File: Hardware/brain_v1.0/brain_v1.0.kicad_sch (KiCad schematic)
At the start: 77 parts, among them J1 Conn_01x02, J10 RFID, J11 Conn_01x04, J12 Conn_01x04, J15 Conn_01x05, J2 Conn_01x02, J3 Conn_01x03, J4 JTAG, J5 Conn_01x02, J6 UART, J7 Conn_01x03, J8 UART Backup, J9 Conn_01x02, Q1 BSS138, Q2 BSS138, Q3 SMD-TRANSISTORS-NPN-25V-500MW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, Q4 SMD-TRANSISTORS-NPN-25V-500MW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, Q5 BSS138, Q6 BSS138, SW1 SW_Push, SW2 SW_Push, U1 ESP32-WROOM-32E 4MB, U2 NAU7802SGI

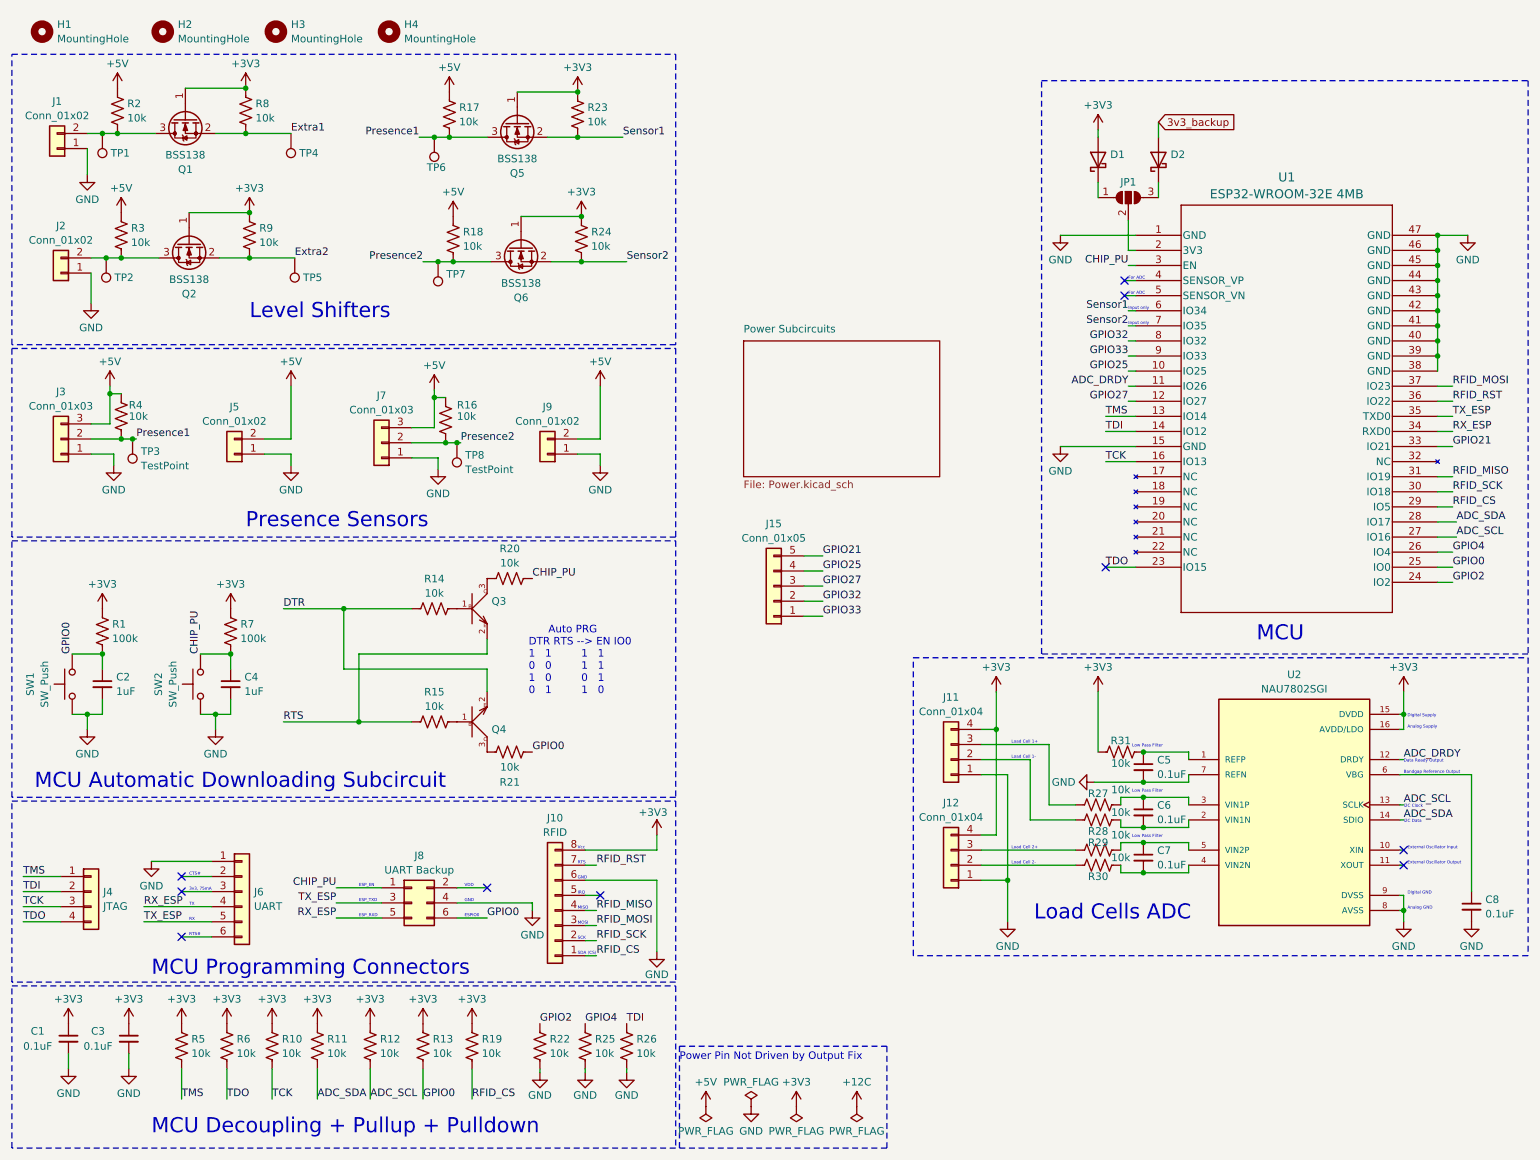
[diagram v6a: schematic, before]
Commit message: made motor driver layout base and moved brain power to a separate board
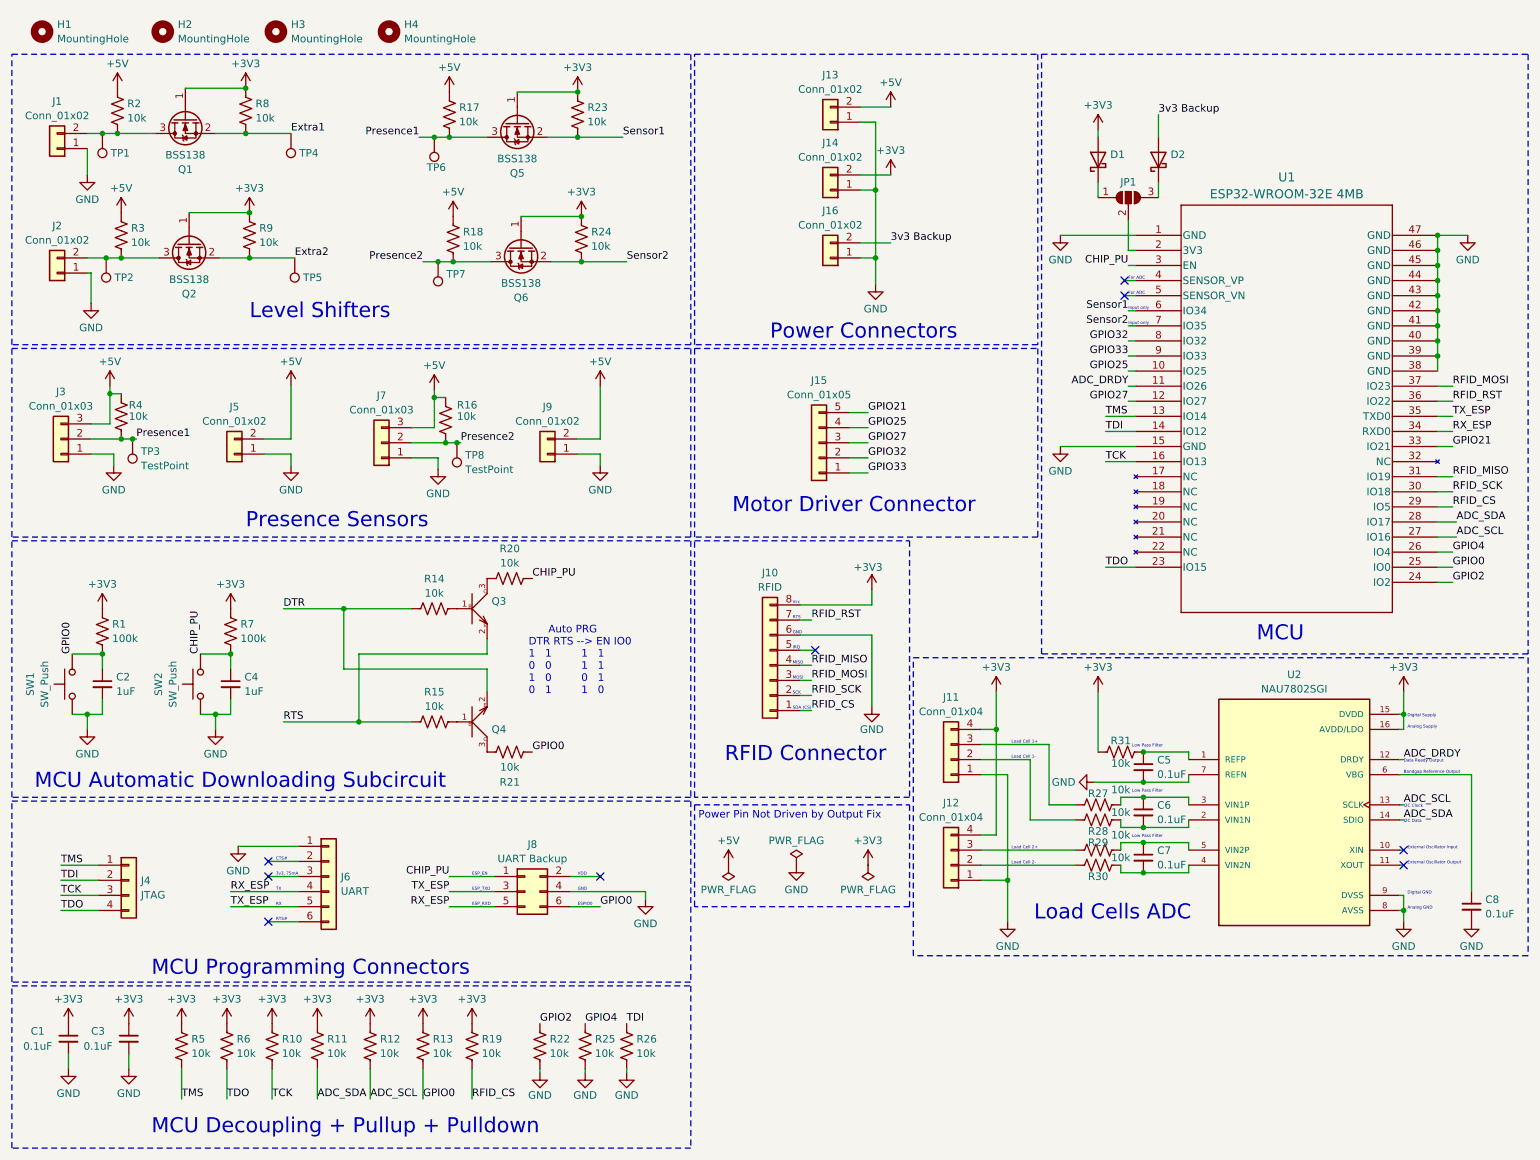
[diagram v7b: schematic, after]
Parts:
- added J13, J14, J16: Conn_01x02, Connector_Molex:Molex_KK-254_AE-6410-02A_1x02_P2.54mm_Vertical, symbol Connector_Generic:Conn_01x02
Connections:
- net +3V3: now also J14.2 (Pin_2)
- net +5V: now also J13.2 (Pin_2)
- net GND: now also J13.1 (Pin_1), J14.1 (Pin_1), J16.1 (Pin_1)
- net 3v3_backup renamed 3v3 Backup
- net 3v3 Backup: now also J16.2 (Pin_2)
- no-connect marks 10 -> 9
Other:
- removed sheet Power Subcircuits
- note added: "Motor Driver Connector"
- note added: "Power Connectors"
- note added: "RFID Connector"
- moved on the sheet: J10, J15, J2, J4, J6, J8

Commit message: started brain layout, can definitely be done in the 100x100 mm space
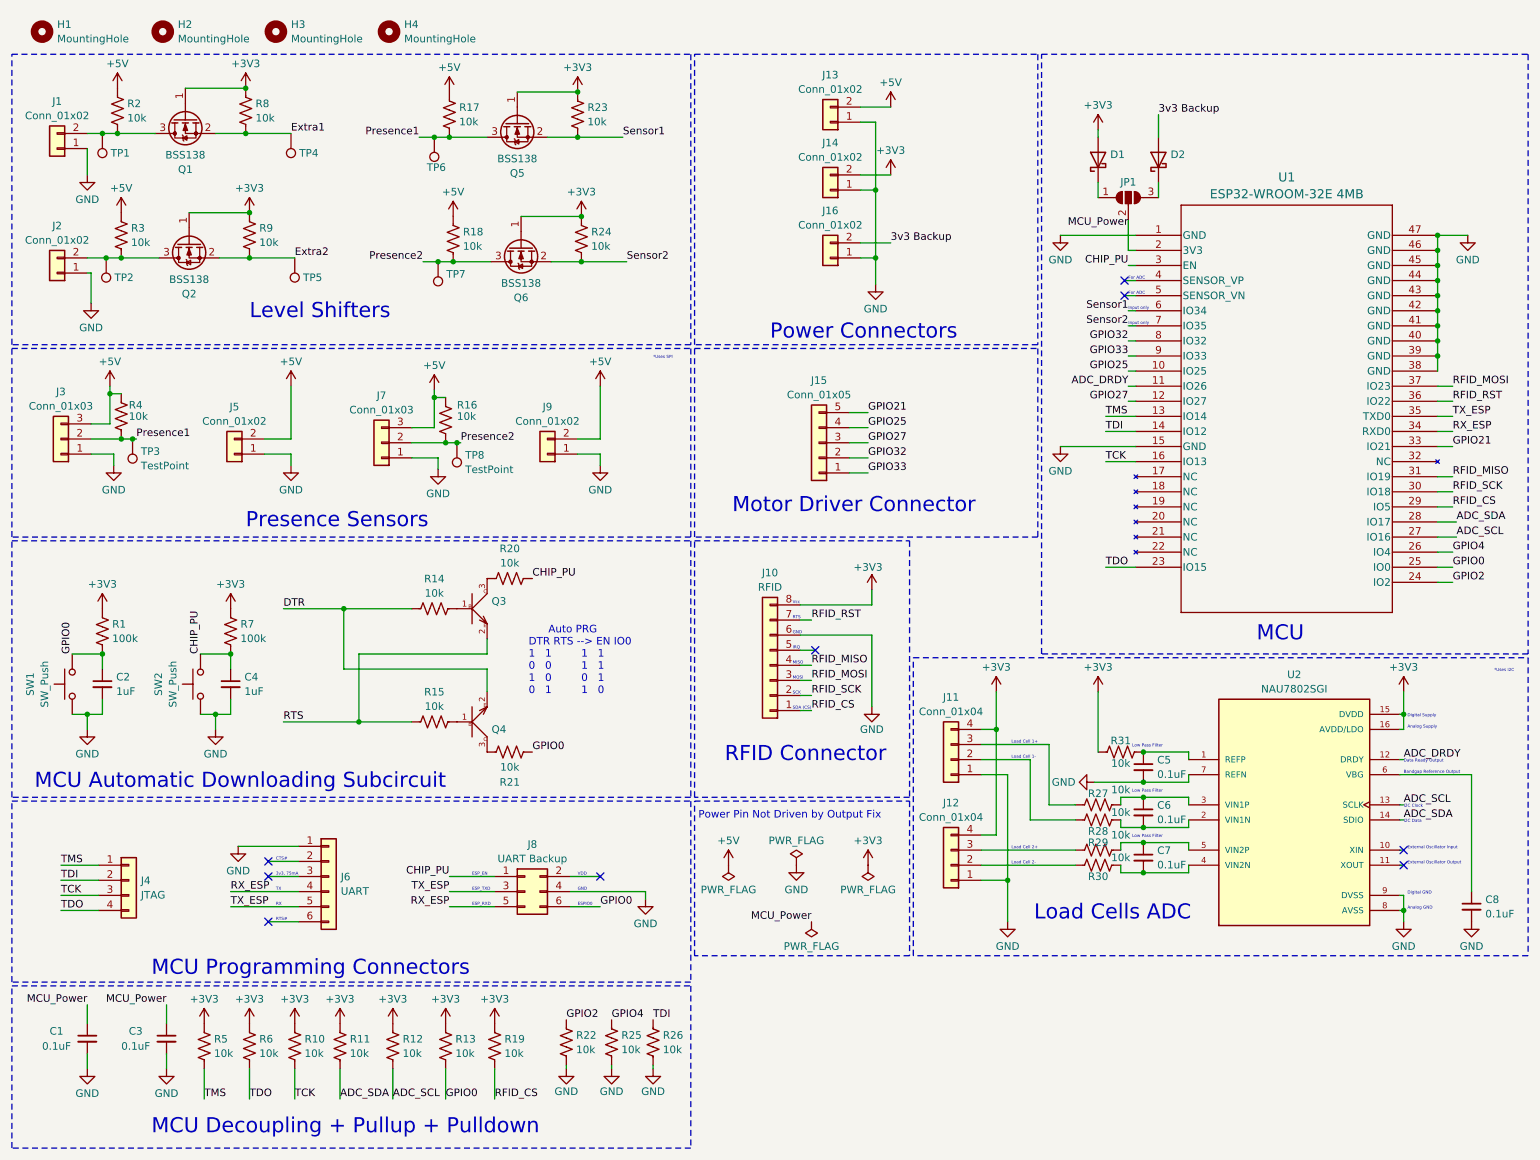
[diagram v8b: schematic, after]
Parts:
- Q3, Q4: footprint SMD-TRANSISTORS-NPN-25V-500MW_SOT-23_:SOT-23 -> S8050:S8050-SMD
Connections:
- net +3V3: no longer C1.1, C3.1
- net MCU_Power: now reaches JP1.2 (C), U1.2 (3V3)
- net MCU_Power: now also C1.1, C3.1
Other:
- note added: "*Uses I2C"
- note added: "*Uses SPI"
- moved on the sheet: C1, C3, R10, R11, R12, R13, R19, R22, R25, R26, R5, R6
